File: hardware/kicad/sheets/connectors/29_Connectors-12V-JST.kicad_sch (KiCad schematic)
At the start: 35 parts

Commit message: reorganized
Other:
- title: Connectors-12V-JST -> 12V JST Outputs

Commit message: before final cleanup
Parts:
- renumbered -12V+_2 to -12V+_1, -12V+_1 to -12V+_2, C145 to C100, C144 to C101, C143 to C102, C130 to C103, C129 to C104, C128 to C105, C127 to C106, C125 to C96, C126 to C97, C69 to C98, C68 to C99, CUR_1 to CUR_3, D17 to D27, D16 to D28, D18 to D29, R521 to R143, R288 to R144, R289 to R145, R144 to R146, R145 to R147, R71 to R148, R146 to R149, R147 to R150, R286 to R151, R287 to R152, R520 to R153, R148 to R154, R149 to R155, R285 to R156, R284 to R157, R522 to R158

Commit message: imrpved footprints
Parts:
- -12V+_1, -12V+_2, -12V+_3: footprint 5v rail sm-easyedapro:CONN-TH_2P-P3.96_VH3.96-2AW -> Connector_JST:JST_VH_B2P-VH_1x02_P3.96mm_Vertical
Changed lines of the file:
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@@
 			)
 		)
-		(property "Footprint" "5v rail sm-easyedapro:CONN-TH_2P-P3.96_VH3.96-2AW"
+		(property "Footprint" "Connector_JST:JST_VH_B2P-VH_1x02_P3.96mm_Vertical"
 			(at 284.48 36.83 0)
 			(effects
@@
 			)
 		)
-		(property "Footprint" "5v rail sm-easyedapro:CONN-TH_2P-P3.96_VH3.96-2AW"
+		(property "Footprint" "Connector_JST:JST_VH_B2P-VH_1x02_P3.96mm_Vertical"
 			(at 363.22 130.81 0)
 			(effects
@@
 			)
 		)
-		(property "Footprint" "5v rail sm-easyedapro:CONN-TH_2P-P3.96_VH3.96-2AW"
+		(property "Footprint" "Connector_JST:JST_VH_B2P-VH_1x02_P3.96mm_Vertical"
 			(at 22.86 146.05 0)
 			(effects

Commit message: added better footprints and steps
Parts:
- removed -12V+_1, -12V+_2, -12V+_3: VH3.96-2P WZ, Connector_JST:JST_VH_B2P-VH_1x02_P3.96mm_Vertical, symbol 5v rail sm-easyedapro:VH3.96-2P WZ
- added U32, U70, U71: VH3_96-2P_WZ, JLCImport:VH3_96-2P_WZ, symbol JLCImport:VH3_96-2P_WZ
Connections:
- net GND: now also U32.1, U70.1, U71.1
- net at C103.2, C104.2, D28.1 (K)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: now also U70.2
- net at C96.2, C97.2, D27.1 (K)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: now also U32.2
- net at C105.2, C106.2, D29.1 (K)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: now also U71.2

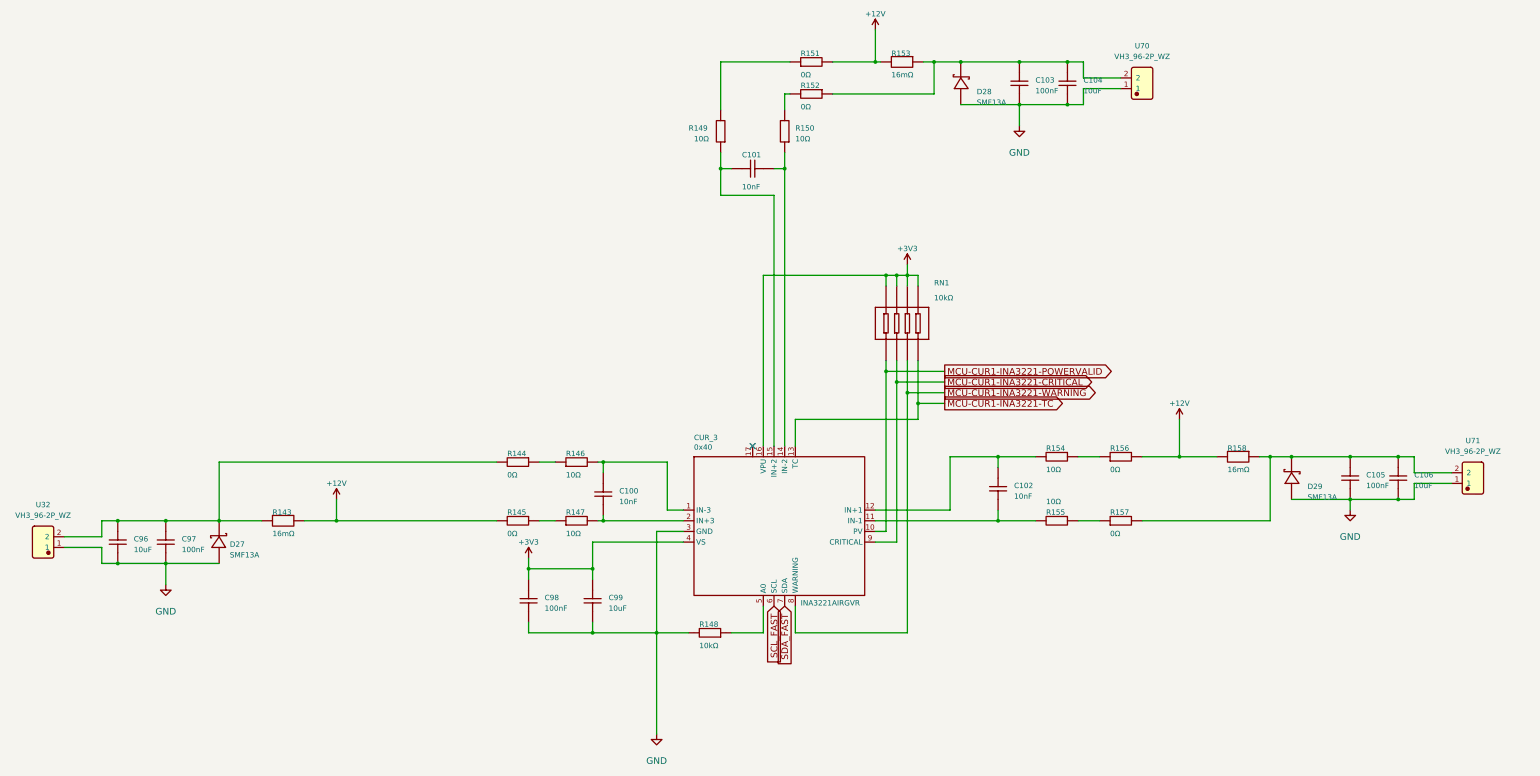
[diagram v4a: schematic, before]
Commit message: netties and better sheet nesting for servo connectors
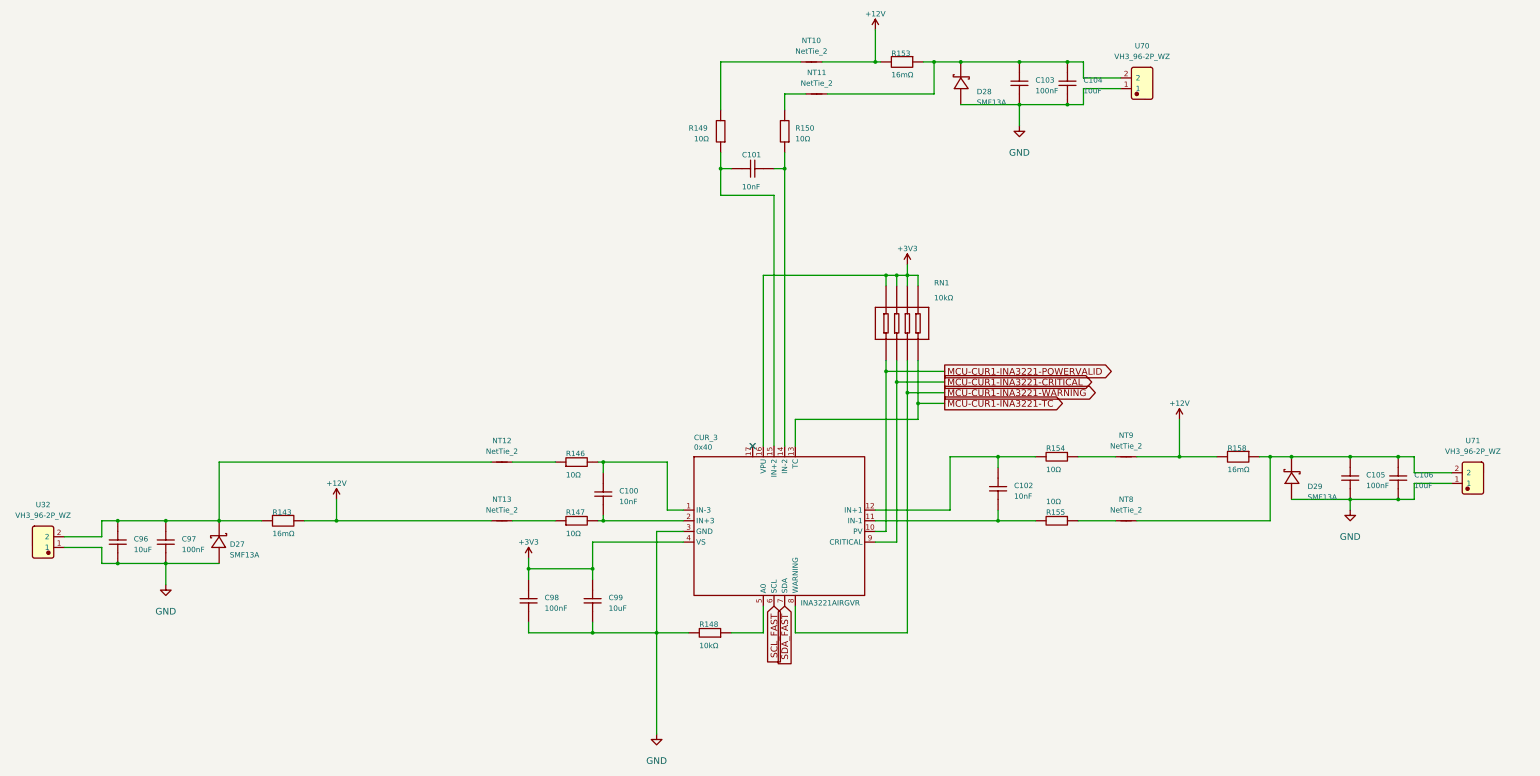
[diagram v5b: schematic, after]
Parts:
- removed R144, R145, R151, R152, R156, R157: 0Ω, Resistor_SMD:R_0201_0603Metric, symbol 5v rail sm-easyedapro:RC0201FR-070RL
- added NT10, NT11, NT12, NT13, NT8, NT9: NetTie_2, 5v rail sm-easyedapro:NetTie-2_SMD_Pad0.2mm, symbol Device:NetTie_2
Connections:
- net +12V: now also NT10.2, NT13.1, NT9.2
- net at C103.2, C104.2, D28.1 (K)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: now also NT11.2
- net at R150.2: now also NT11.1
- net at R147.1: now also NT13.2
- net at C96.2, C97.2, D27.1 (K)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: now also NT12.1
- net at R146.1: now also NT12.2
- net at C105.2, C106.2, D29.1 (K)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: now also NT8.2
- net at R154.1: now also NT9.1
- net at R149.2: now also NT10.1
- net at R155.1: now also NT8.1

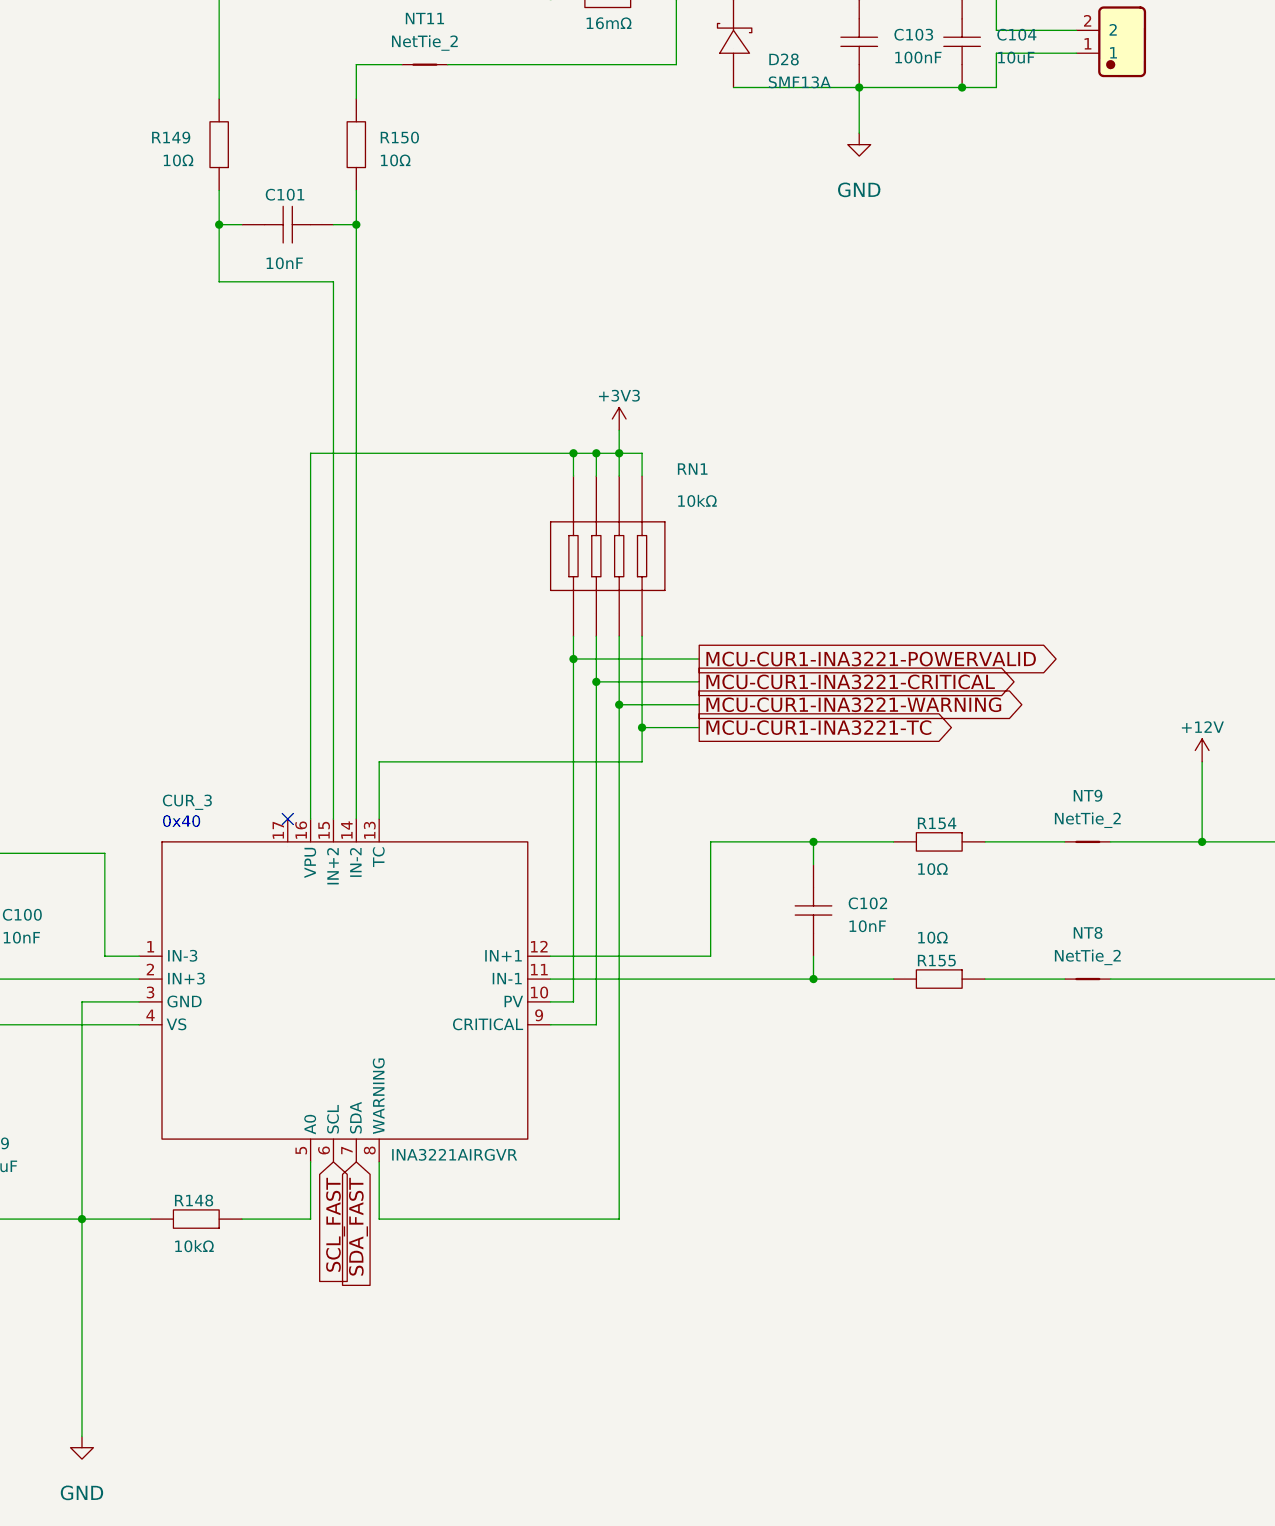
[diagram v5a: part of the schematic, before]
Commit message: clearer power path with sheets
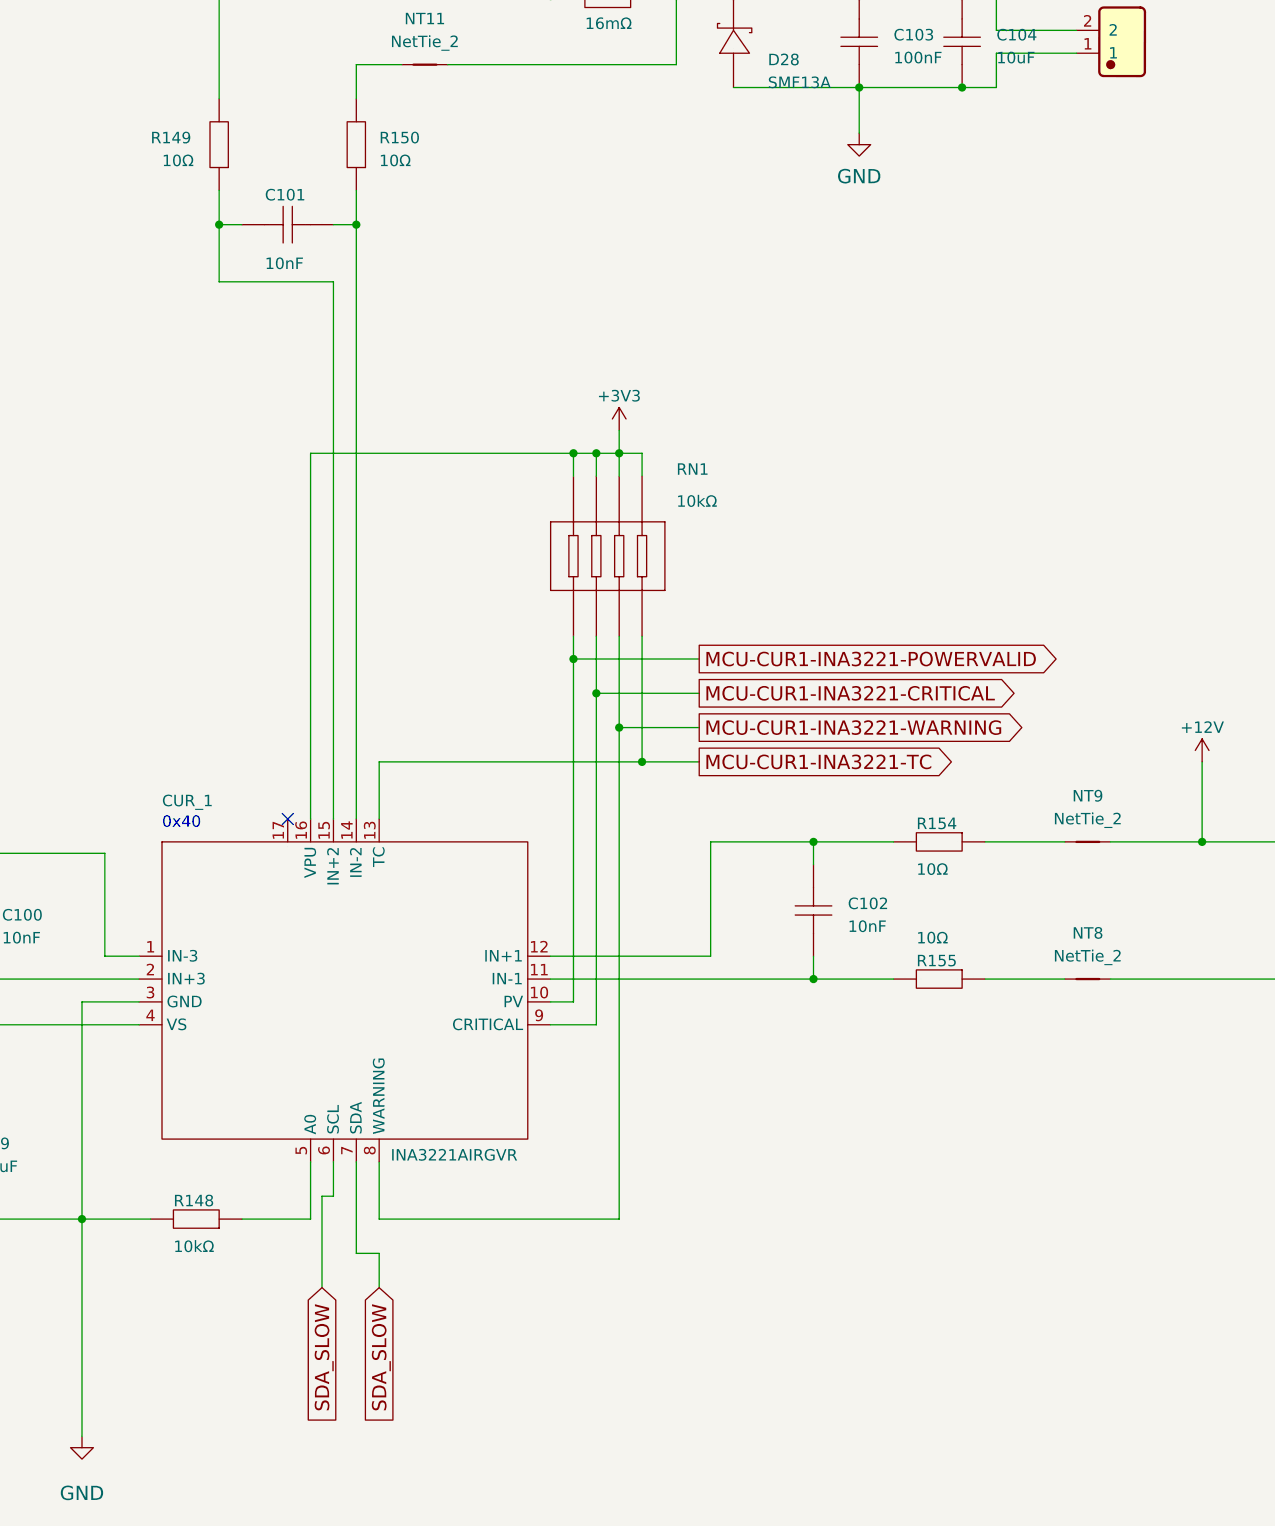
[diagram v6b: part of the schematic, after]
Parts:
- renumbered CUR_3 to CUR_1
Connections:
- net SDA_FAST is gone; now on net SDA_SLOW: CUR_1.7 (SDA)
- net SCL_FAST renamed SDA_SLOW
